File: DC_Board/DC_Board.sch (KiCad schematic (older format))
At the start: 34 parts, among them J1 0039281243, J10 15-24-4449, J11 Conn_01x03_Male, J12 Conn_01x02_Male, J13 Conn_01x02_Male, J2 0039281243, J3 26-01-3115, J4 26-01-3115, J5 26-01-3115, J6 26-01-3115, J7 15-24-4449, J8 15-24-4449, J9 15-24-4449, K1 EC2-12NU, Q1 BC547, Q2 FQP30N06L, U1 ATtiny

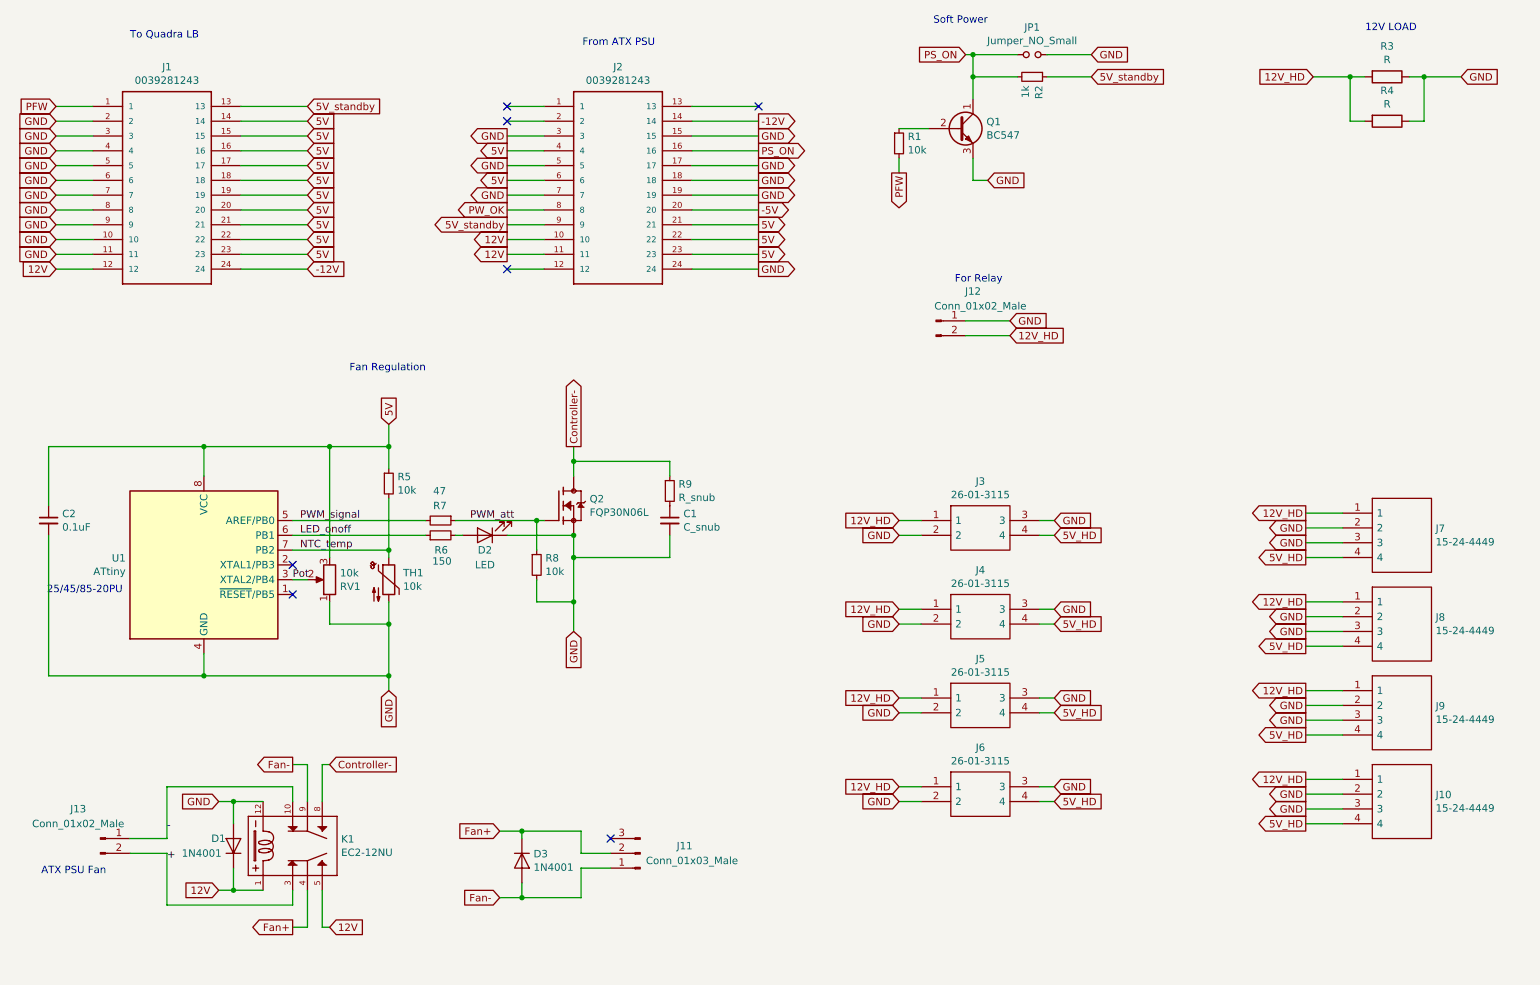
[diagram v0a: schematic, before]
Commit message: Brand new AC and DC boards
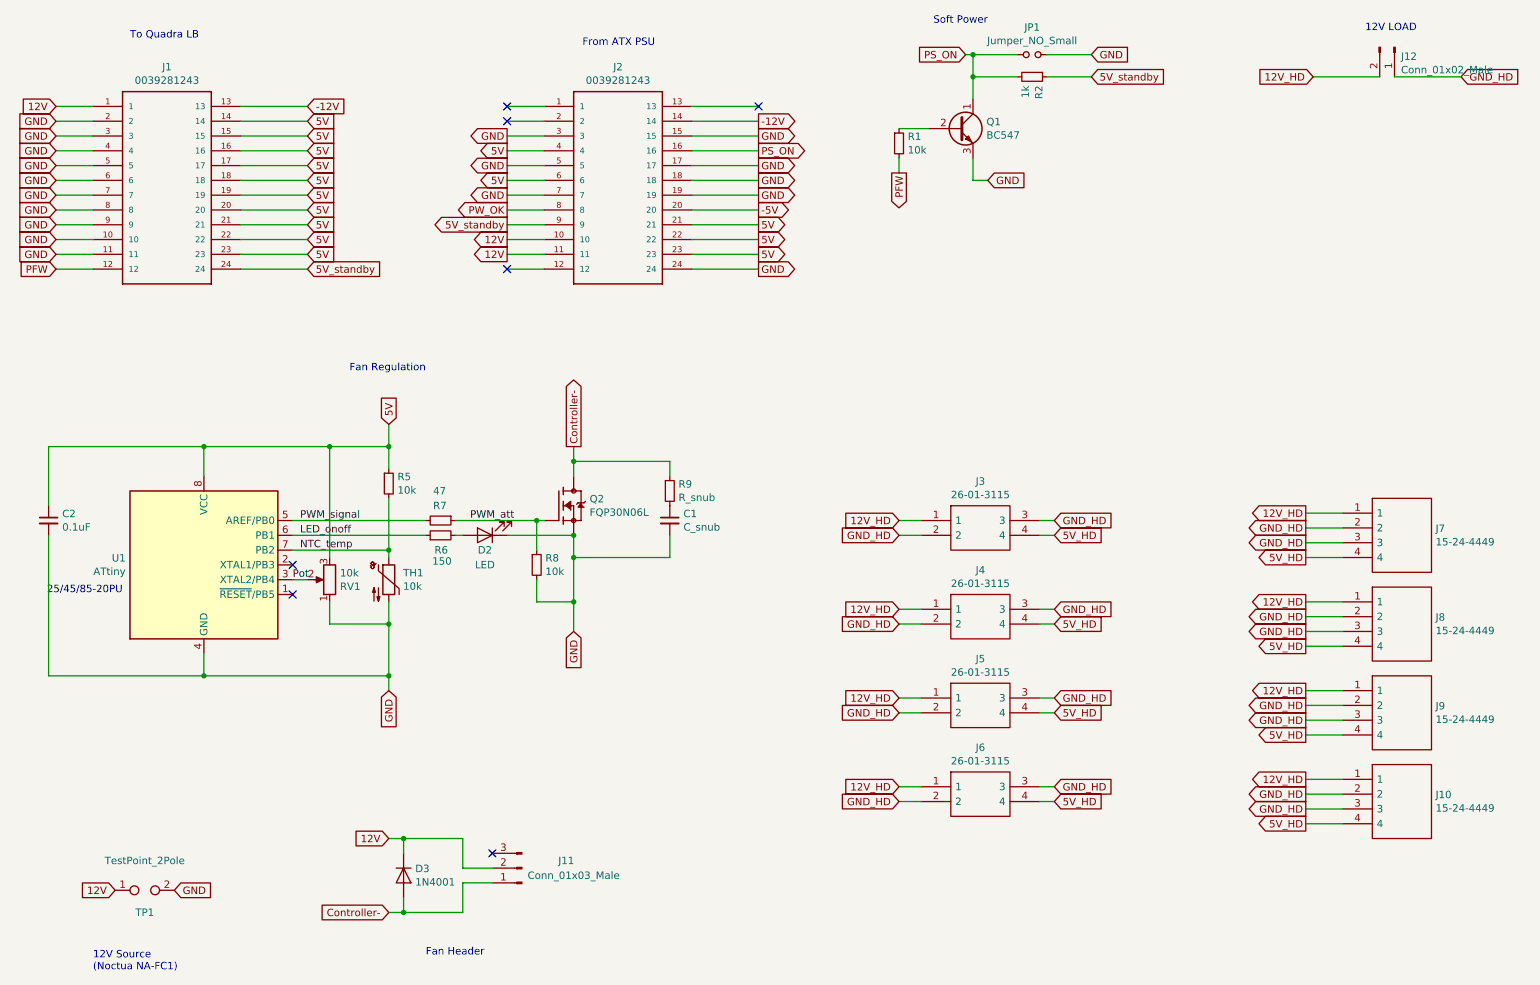
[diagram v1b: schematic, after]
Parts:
- removed D1: 1N4001, Diode_THT:D_DO-41_SOD81_P10.16mm_Horizontal, symbol Diode:1N4001
- removed J13: Conn_01x02_Male, Connector_Molex:Molex_KK-254_AE-6410-02A_1x02_P2.54mm_Vertical, symbol Connector:Conn_01x02_Male
- removed K1: EC2-12NU, Relay_12:RELAY_EC2-5NU, symbol Relay_12:EC2-5NU
- removed R3, R4: R, Resistor_THT:R_Axial_Power_L38.0mm_W9.0mm_P45.72mm, symbol Device:R
- added TP1: TestPoint_2Pole, Connector_PinHeader_2.54mm:PinHeader_2x01_P2.54mm_Vertical, symbol Connector:TestPoint_2Pole
- J1: footprint Connector_Molex:Molex_Mini-Fit_Jr_5566-24A_2x12_P4.20mm_Vertical -> Connector_Molex:Molex_Mini-Fit_Jr_5566-24A2_2x12_P4.20mm_Vertical
- J10, J7, J8, J9: footprint Connector_TE-Connectivity:TE_MATE-N-LOK_350211-1_1x04_P5.08mm_Vertical -> Molex_Right_Angle:641737-1
- J12: footprint Connector_Molex:Molex_KK-254_AE-6410-02A_1x02_P2.54mm_Vertical -> Connector_Molex:Molex_KK-396_A-41791-0002_1x02_P3.96mm_Vertical
- TH1: footprint Connector_PinHeader_2.54mm:PinHeader_1x02_P2.54mm_Vertical -> Resistor_THT:R_Axial_DIN0309_L9.0mm_D3.2mm_P15.24mm_Horizontal
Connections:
- net Fan+ is gone; now on net 12V: D3.1 (K), J11.2 (Pin_2)
- net Fan- is gone; now on net Controller-: D3.2 (A), J11.1 (Pin_1)
- net -12V: now also J1.13; no longer J1.24
- net 12V: now also J1.1, TP1.1; no longer J1.12
- net 5V_standby: now also J1.24; no longer J1.13
- net GND: now also TP1.2; no longer J10.2, J10.3, J12.1 (Pin_1), J3.2, J3.3, J4.2, J4.3, J5.2, J5.3, J6.2, J6.3, J7.2, J7.3, J8.2, J8.3, J9.2, J9.3
- net PFW: now also J1.12; no longer J1.1
- new net GND_HD: J10.2, J10.3, J12.1 (Pin_1), J3.2, J3.3, J4.2, J4.3, J5.2, J5.3, J6.2, J6.3, J7.2, J7.3, J8.2, J8.3, J9.2, J9.3
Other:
- note added: "12V Source\n(Noctua NA-FC1)"
- note added: "Fan Header"
- note removed: "ATX PSU Fan"
- note removed: "For Relay"
- moved on the sheet: D3, J11
